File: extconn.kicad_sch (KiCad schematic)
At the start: 22 parts, among them J1401 Conn_02x10_Odd_Even, U1401 74AVC4T245PW, U1402 74AVC4T245PW

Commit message: Schematic: yet another update -Improve way caps are specified once again -Update cap voltages based on ESD simulation -Make anti-aliasing LC filter more practical - with much less inductors -Specify Mfr & MfrPN for almost all components (most from Mouser, some from Digikey)
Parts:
- C1401, C1402, C1403, C1405, C1406: Mfr (none) -> Samsung; Mfr PN (none) -> CL21B104KBFNNNE
- C1404: Mfr (none) -> Murata; Mfr PN (none) -> GRM21BR71C475ME51
- FB1401: Mfr (none) -> Wurth; Mfr PN (none) -> 782853701
- J1401: Mfr (none) -> Amphenol; Mfr PN (none) -> T821120A1S100CEU
- RN1401, RN1402, RN1403, RN1404: footprint (none) -> Resistor_SMD:R_Array_Convex_4x0603; Mfr (none) -> Bourns; Mfr PN (none) -> CAY16-820J4LF; Tolerance 5% -> (none)
- U1401, U1402: Mfr (none) -> Nexperia; Mfr PN (none) -> 74AVC4T245PW-Q100J
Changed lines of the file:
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@@
+      (effects (font (size 1.27 1.27)) hide)
+    )
+    (property "Mfr" "Samsung" (id 7) (at 190.5 43.18 0)
+      (effects (font (size 1.27 1.27)) hide)
+    )
+    (property "Mfr PN" "CL21B104KBFNNNE" (id 8) (at 190.5 43.18 0)
       (effects (font (size 1.27 1.27)) hide)
     )
@@
     )
     (property "Datasheet" "~" (id 3) (at 176.53 125.73 0)
+      (effects (font (size 1.27 1.27)) hide)
+    )
+    (property "Mfr" "Amphenol" (id 4) (at 176.53 125.73 0)
+      (effects (font (size 1.27 1.27)) hide)
+    )
+    (property "Mfr PN" "T821120A1S100CEU" (id 5) (at 176.53 125.73 0)
       (effects (font (size 1.27 1.27)) hide)
     )
@@
       (effects (font (size 1.27 1.27)) hide)
     )
+    (property "Mfr" "Samsung" (id 7) (at 251.46 43.18 0)
+      (effects (font (size 1.27 1.27)) hide)
+    )
+    (property "Mfr PN" "CL21B104KBFNNNE" (id 8) (at 251.46 43.18 0)
+      (effects (font (size 1.27 1.27)) hide)
+    )
     (pin "1")
     (pin "2")
@@
       (effects (font (size 1.27 1.27)) hide)
     )
+    (property "Mfr" "Wurth" (id 4) (at 228.6 38.1 0)
+      (effects (font (size 1.27 1.27)) hide)
+    )
+    (property "Mfr PN" "782853701" (id 5) (at 228.6 38.1 0)
+      (effects (font (size 1.27 1.27)) hide)
+    )
     (pin "1")
     (pin "2")
@@
     (property "Reference" "RN1403" (id 0) (at 127 94.0902 90))
     (property "Value" "4x82R" (id 1) (at 127 96.6271 90))
-    (property "Footprint" "" (id 2) (at 127 111.125 90)
+    (property "Footprint" "Resistor_SMD:R_Array_Convex_4x0603" (id 2) (at 127 111.125 90)
       (effects (font (size 1.27 1.27)) hide)
     )
@@
       (effects (font (size 1.27 1.27)) hide)
     )
-    (property "Tolerance" "5%" (id 4) (at 127 104.14 0)
+    (property "Tolerance" "" (id 4) (at 127 104.14 0)
+      (effects (font (size 1.27 1.27)) hide)
+    )
+    (property "Mfr" "Bourns" (id 5) (at 127 104.14 0)
+      (effects (font (size 1.27 1.27)) hide)
+    )
+    (property "Mfr PN" "CAY16-820J4LF" (id 6) (at 127 104.14 0)
       (effects (font (size 1.27 1.27)) hide)
     )
@@
     (property "Reference" "RN1404" (id 0) (at 127 142.3502 90))
     (property "Value" "4x82R" (id 1) (at 127 144.8871 90))
-    (property "Footprint" "" (id 2) (at 127 159.385 90)
+    (property "Footprint" "Resistor_SMD:R_Array_Convex_4x0603" (id 2) (at 127 159.385 90)
       (effects (font (size 1.27 1.27)) hide)
     )
@@
       (effects (font (size 1.27 1.27)) hide)
     )
-    (property "Tolerance" "5%" (id 4) (at 127 152.4 0)
+    (property "Tolerance" "" (id 4) (at 127 152.4 0)
+      (effects (font (size 1.27 1.27)) hide)
+    )
+    (property "Mfr" "Bourns" (id 5) (at 127 152.4 0)
+      (effects (font (size 1.27 1.27)) hide)
+    )
+    (property "Mfr PN" "CAY16-820J4LF" (id 6) (at 127 152.4 0)
       (effects (font (size 1.27 1.27)) hide)
     )
@@
     (property "Reference" "RN1402" (id 0) (at 69.85 142.3502 90))
     (property "Value" "4x82R" (id 1) (at 69.85 144.8871 90))
-    (property "Footprint" "" (id 2) (at 69.85 159.385 90)
+    (property "Footprint" "Resistor_SMD:R_Array_Convex_4x0603" (id 2) (at 69.85 159.385 90)
       (effects (font (size 1.27 1.27)) hide)
     )
@@
       (effects (font (size 1.27 1.27)) hide)
     )
-    (property "Tolerance" "5%" (id 4) (at 69.85 152.4 0)
+    (property "Tolerance" "" (id 4) (at 69.85 152.4 0)
+      (effects (font (size 1.27 1.27)) hide)
+    )
+    (property "Mfr" "Bourns" (id 5) (at 69.85 152.4 0)
+      (effects (font (size 1.27 1.27)) hide)
+    )
+    (property "Mfr PN" "CAY16-820J4LF" (id 6) (at 69.85 152.4 0)
       (effects (font (size 1.27 1.27)) hide)
     )
@@
     )
     (property "Datasheet" "https://www.ti.com/lit/ds/symlink/sn74avc4t245.pdf" (id 3) (at 97.79 151.13 0)
+      (effects (font (size 1.27 1.27)) hide)
+    )
+    (property "Mfr" "Nexperia" (id 4) (at 99.06 144.78 0)
+      (effects (font (size 1.27 1.27)) hide)
+    )
+    (property "Mfr PN" "74AVC4T245PW-Q100J" (id 5) (at 99.06 144.78 0)
       (effects (font (size 1.27 1.27)) hide)
     )
@@
     (property "Reference" "RN1401" (id 0) (at 69.85 94.0902 90))
     (property "Value" "4x82R" (id 1) (at 69.85 96.6271 90))
-    (property "Footprint" "" (id 2) (at 69.85 111.125 90)
+    (property "Footprint" "Resistor_SMD:R_Array_Convex_4x0603" (id 2) (at 69.85 111.125 90)
       (effects (font (size 1.27 1.27)) hide)
     )
@@
       (effects (font (size 1.27 1.27)) hide)
     )
-    (property "Tolerance" "5%" (id 4) (at 69.85 104.14 0)
+    (property "Tolerance" "" (id 4) (at 69.85 104.14 0)
+      (effects (font (size 1.27 1.27)) hide)
+    )
+    (property "Mfr" "Bourns" (id 5) (at 69.85 104.14 0)
+      (effects (font (size 1.27 1.27)) hide)
+    )
+    (property "Mfr PN" "CAY16-820J4LF" (id 6) (at 69.85 104.14 0)
       (effects (font (size 1.27 1.27)) hide)
     )
@@
       (effects (font (size 1.27 1.27)) hide)
     )
+    (property "Mfr" "Samsung" (id 7) (at 264.16 43.18 0)
+      (effects (font (size 1.27 1.27)) hide)
+    )
+    (property "Mfr PN" "CL21B104KBFNNNE" (id 8) (at 264.16 43.18 0)
+      (effects (font (size 1.27 1.27)) hide)
+    )
     (pin "1")
     (pin "2")
@@
     )
     (property "Tolerance" "" (id 6) (at 177.8 43.18 0)
+      (effects (font (size 1.27 1.27)) hide)
+    )
+    (property "Mfr" "Samsung" (id 7) (at 177.8 43.18 0)
+      (effects (font (size 1.27 1.27)) hide)
+    )
+    (property "Mfr PN" "CL21B104KBFNNNE" (id 8) (at 177.8 43.18 0)
       (effects (font (size 1.27 1.27)) hide)
     )
@@
     )
     (property "Datasheet" "https://www.ti.com/lit/ds/symlink/sn74avc4t245.pdf" (id 3) (at 97.79 102.87 0)
+      (effects (font (size 1.27 1.27)) hide)
+    )
+    (property "Mfr" "Nexperia" (id 4) (at 99.06 96.52 0)
+      (effects (font (size 1.27 1.27)) hide)
+    )
+    (property "Mfr PN" "74AVC4T245PW-Q100J" (id 5) (at 99.06 96.52 0)
       (effects (font (size 1.27 1.27)) hide)
     )
@@
       (effects (font (size 1.27 1.27)) hide)
     )
+    (property "Mfr" "Samsung" (id 7) (at 215.9 43.18 0)
+      (effects (font (size 1.27 1.27)) hide)
+    )
+    (property "Mfr PN" "CL21B104KBFNNNE" (id 8) (at 215.9 43.18 0)
+      (effects (font (size 1.27 1.27)) hide)
+    )
     (pin "1")
     (pin "2")
@@
       (effects (font (size 1.27 1.27)) hide)
     )
+    (property "Mfr" "Murata" (id 7) (at 238.76 43.18 0)
+      (effects (font (size 1.27 1.27)) hide)
+    )
+    (property "Mfr PN" "GRM21BR71C475ME51" (id 8) (at 238.76 43.18 0)
+      (effects (font (size 1.27 1.27)) hide)
+    )

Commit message: Schematic: add PNs for resistors
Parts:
- R1401, R1403, R1405, R1408: Mfr (none) -> Bourns; Mfr PN (none) -> CR0805-J/-000ELF
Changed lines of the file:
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@@
+      (effects (font (size 1.27 1.27)) hide)
+    )
+    (property "Mfr" "Bourns" (id 4) (at 127 55.88 0)
+      (effects (font (size 1.27 1.27)) hide)
+    )
+    (property "Mfr PN" "CR0805-J/-000ELF" (id 5) (at 127 55.88 0)
       (effects (font (size 1.27 1.27)) hide)
     )
@@
     )
     (property "Datasheet" "~" (id 3) (at 69.85 45.72 0)
+      (effects (font (size 1.27 1.27)) hide)
+    )
+    (property "Mfr" "Bourns" (id 4) (at 69.85 45.72 0)
+      (effects (font (size 1.27 1.27)) hide)
+    )
+    (property "Mfr PN" "CR0805-J/-000ELF" (id 5) (at 69.85 45.72 0)
       (effects (font (size 1.27 1.27)) hide)
     )
@@
       (effects (font (size 1.27 1.27)) hide)
     )
+    (property "Mfr" "Bourns" (id 4) (at 88.9 45.72 0)
+      (effects (font (size 1.27 1.27)) hide)
+    )
+    (property "Mfr PN" "CR0805-J/-000ELF" (id 5) (at 88.9 45.72 0)
+      (effects (font (size 1.27 1.27)) hide)
+    )
     (pin "1")
     (pin "2")
@@
       (effects (font (size 1.27 1.27)) hide)
     )
+    (property "Mfr" "Bourns" (id 4) (at 107.95 45.72 0)
+      (effects (font (size 1.27 1.27)) hide)
+    )
+    (property "Mfr PN" "CR0805-J/-000ELF" (id 5) (at 107.95 45.72 0)
+      (effects (font (size 1.27 1.27)) hide)
+    )

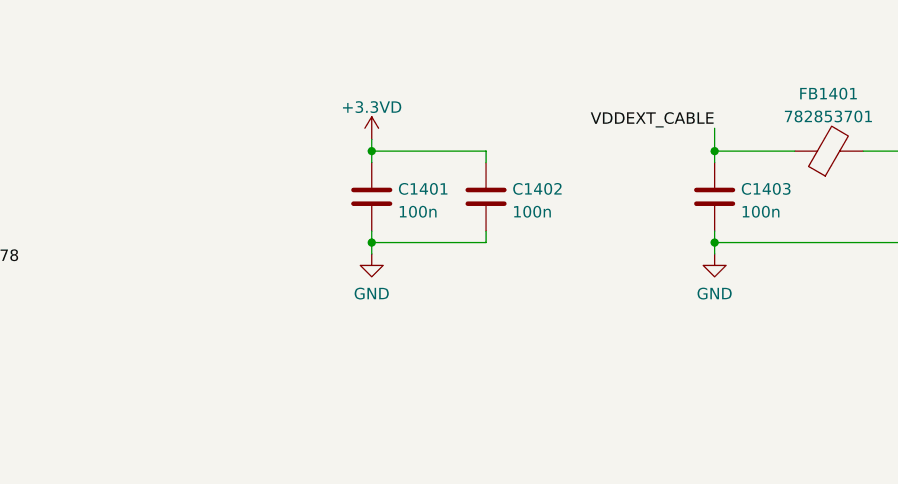
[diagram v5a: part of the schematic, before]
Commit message: Add 3v3 TVS to extconn VDD supply rail
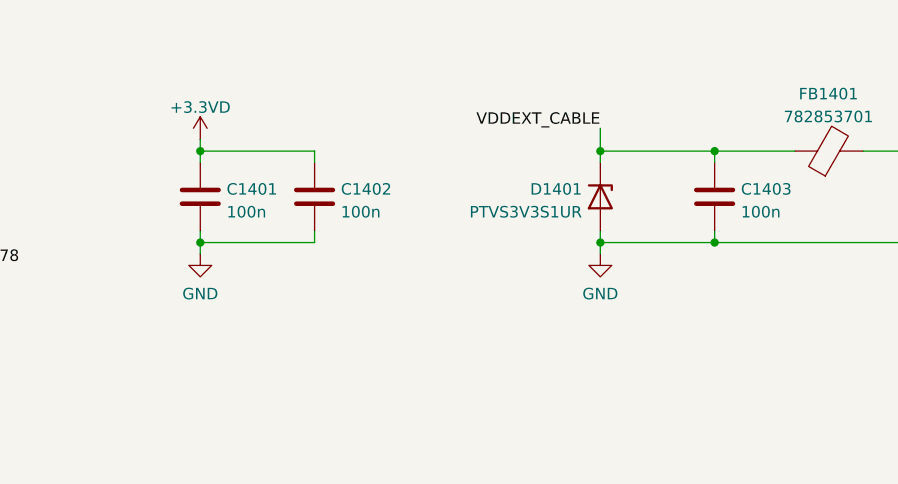
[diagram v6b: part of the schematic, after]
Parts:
- added D1401: PTVS3V3S1UR, Diode_SMD:D_SOD-123, symbol Device:D_Zener
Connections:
- net GND: now also D1401.2 (A)
- net VDDEXT_CABLE: now also D1401.1 (K)
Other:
- moved on the sheet: C1401, C1402

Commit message: Update footprints: - SOD323F, SOD323, SOD123W... intead of generic handsolder version - 3225 xtal - use handsolder footprint - do not use handsolder version for ferrite beads - use SOT-23-6 instead of TSOP-6
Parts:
- D1401: footprint Diode_SMD:D_SOD-123 -> Diode_SMD:Nexperia_CFP3_SOD-123W
- FB1401: footprint Inductor_SMD:L_0805_2012Metric_Pad1.05x1.20mm_HandSolder -> Inductor_SMD:L_0805_2012Metric
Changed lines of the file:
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@@
       (effects (font (size 1.27 1.27)) (justify right))
     )
-    (property "Footprint" "Diode_SMD:D_SOD-123" (id 2) (at 203.2 43.18 0)
+    (property "Footprint" "Diode_SMD:Nexperia_CFP3_SOD-123W" (id 2) (at 203.2 43.18 0)
       (effects (font (size 1.27 1.27)) hide)
     )
@@
     (property "Reference" "FB1401" (id 0) (at 228.5492 31.7586 90))
     (property "Value" "782853701" (id 1) (at 228.5492 34.2955 90))
-    (property "Footprint" "Inductor_SMD:L_0805_2012Metric_Pad1.05x1.20mm_HandSolder" (id 2) (at 228.6 39.878 90)
+    (property "Footprint" "Inductor_SMD:L_0805_2012Metric" (id 2) (at 228.6 39.878 90)
       (effects (font (size 1.27 1.27)) hide)
     )

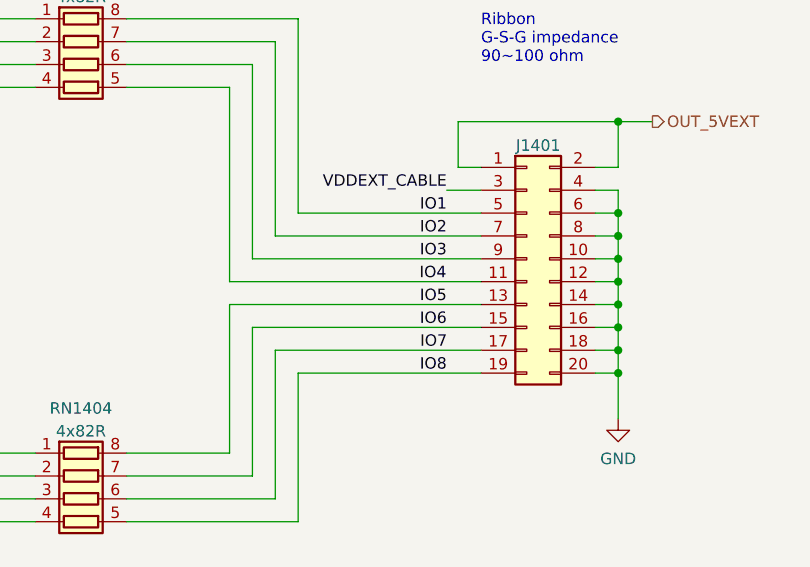
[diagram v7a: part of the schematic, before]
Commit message: ExtConn: fix bug in net naming
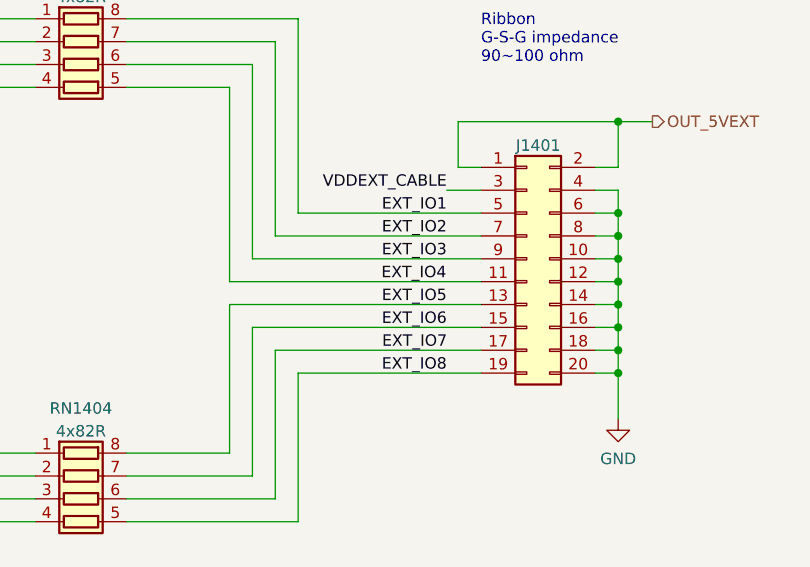
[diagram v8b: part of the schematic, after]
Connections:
- net IO1: no longer J1401.5 (Pin_5), RN1403.8 (R1.2)
- net IO2: no longer J1401.7 (Pin_7), RN1403.7 (R2.2)
- net IO3: no longer J1401.9 (Pin_9), RN1403.6 (R3.2)
- net IO4: no longer J1401.11 (Pin_11), RN1403.5 (R4.2)
- net IO5: no longer J1401.13 (Pin_13), RN1404.8 (R1.2)
- net IO6: no longer J1401.15 (Pin_15), RN1404.7 (R2.2)
- net IO7: no longer J1401.17 (Pin_17), RN1404.6 (R3.2)
- net IO8: no longer J1401.19 (Pin_19), RN1404.5 (R4.2)
- new net EXT_IO1: J1401.5 (Pin_5), RN1403.8 (R1.2)
- new net EXT_IO2: J1401.7 (Pin_7), RN1403.7 (R2.2)
- new net EXT_IO3: J1401.9 (Pin_9), RN1403.6 (R3.2)
- new net EXT_IO4: J1401.11 (Pin_11), RN1403.5 (R4.2)
- new net EXT_IO5: J1401.13 (Pin_13), RN1404.8 (R1.2)
- new net EXT_IO6: J1401.15 (Pin_15), RN1404.7 (R2.2)
- new net EXT_IO7: J1401.17 (Pin_17), RN1404.6 (R3.2)
- new net EXT_IO8: J1401.19 (Pin_19), RN1404.5 (R4.2)
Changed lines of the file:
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@@
     (effects (font (size 1.27 1.27)) (justify right bottom))
   )
-  (label "IO7" (at 167.6763 135.89 180)
+  (label "EXT_IO7" (at 167.6763 135.89 180)
     (effects (font (size 1.27 1.27)) (justify right bottom))
   )
@@
     (effects (font (size 1.27 1.27)) (justify right bottom))
   )
-  (label "IO3" (at 167.64 125.73 180)
+  (label "EXT_IO3" (at 167.64 125.73 180)
     (effects (font (size 1.27 1.27)) (justify right bottom))
   )
@@
     (effects (font (size 1.27 1.27)) (justify right bottom))
   )
-  (label "IO4" (at 167.5992 128.27 180)
+  (label "EXT_IO4" (at 167.5992 128.27 180)
     (effects (font (size 1.27 1.27)) (justify right bottom))
   )
@@
     (effects (font (size 1.27 1.27)) (justify left bottom))
   )
-  (label "IO8" (at 167.64 138.43 180)
+  (label "EXT_IO8" (at 167.64 138.43 180)
     (effects (font (size 1.27 1.27)) (justify right bottom))
   )
@@
     (effects (font (size 1.27 1.27)) (justify left bottom))
   )
-  (label "IO5" (at 167.64 130.81 180)
+  (label "EXT_IO5" (at 167.64 130.81 180)
     (effects (font (size 1.27 1.27)) (justify right bottom))
   )
-  (label "IO2" (at 167.6499 123.19 180)
+  (label "EXT_IO2" (at 167.6499 123.19 180)
     (effects (font (size 1.27 1.27)) (justify right bottom))
   )
@@
     (effects (font (size 1.27 1.27)) (justify right bottom))
   )
-  (label "IO6" (at 167.64 133.35 180)
+  (label "EXT_IO6" (at 167.64 133.35 180)
     (effects (font (size 1.27 1.27)) (justify right bottom))
   )
@@
     (effects (font (size 1.27 1.27)) (justify left bottom))
   )
-  (label "IO1" (at 167.6499 120.65 180)
+  (label "EXT_IO1" (at 167.6499 120.65 180)
     (effects (font (size 1.27 1.27)) (justify right bottom))
   )
